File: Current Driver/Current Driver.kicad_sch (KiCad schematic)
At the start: 41 parts, among them Q1 BC817, Q2 D45H11G (n_b), Q3 BC807, Q4 D44H11(n_b), SW1 SW_Push, U1 ADA4622-2xCP, U2 ADA4622-2xCP

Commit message: Clean Schematic
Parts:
- removed D3: AS3BJ (n_b), Diode_SMD:D_SOD-523, symbol Diode:1N4148WT
- removed Q4: D44H11(n_b), symbol Simulation_SPICE:PNP
- removed R32, R33: 1kΩ, symbol Device:R
- removed SW1: SW_Push, symbol Switch:SW_Push
- removed unit 2 of U2
- added J1: Conn_01x03, symbol Connector_Generic:Conn_01x03
- added J2: Conn_01x02, symbol Connector_Generic:Conn_01x02
- added J3: Cewka, symbol Connector_Generic:Conn_01x02
- added Q4: NPN, symbol Simulation_SPICE:NPN
- added R22, R25, R27, R28, R29: R, symbol Device:R
- added unit 2 of U1
- renumbered C4 to C1, C6 to C2, C7 to C3, Q3 to Q2, Q2 to Q3, R6 to R1, R19 to R10, R5 to R11, R24 to R12, R12 to R13, R9 to R14, R29 to R15, R1 to R16, R21 to R17, R3 to R18, R18 to R19, R8 to R2, R2 to R20, R20 to R21, R7 to R23, R16 to R24, R28 to R26, R13 to R3, R17 to R30, R9 to R4, R14 to R5, R11 to R6, R15 to R7, R4 to R8, R10 to R9
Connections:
- net +VCC: now also R22.1; no longer Q3.3 (E)
- net +Vop: now also J1.3 (Pin_3)
- net -VCC: now also R25.2
- net -Vop: now also J1.1 (Pin_1)
- net GND: now also R26.2, J1.2 (Pin_2), J2.2 (Pin_2), R27.2, R28.2, R29.2; no longer R26.1, R7.2
- net DRIVING_OUTPUT: now reaches F1.1, R23.2, R24.1
- net DRIVER_OUTPUT: now reaches F1.2, R30.1
- net DRIVER_OUTPUT: now also J3.2 (Pin_2)
- net at Q2.2 (E), R24.2: now also Q4.1 (C)
- net at Q2.3 (C), R21.1: now also Q4.2 (B)
- net at R30.2: now also R15.1, R26.1, J3.1 (Pin_1), R27.1, R28.1, R29.1
- net at C1.2, R8.2, R9.2: now also U2.1; no longer U1.1
- net SIGNAL_INPUT: now reaches R6.1, R7.1
- net SIGNAL_INPUT: now also U2.3 (+); no longer U1.2 (-)
- net V_REF: now reaches C1.1, R4.1, R8.1
- net V_REF: now also U2.2 (-); no longer U1.3 (+)
- net at C2.1, R10.1: now also U1.2 (-); no longer U2.2 (-)
- net at C2.2, R11.1, R13.2: now also U1.1; no longer U2.1
- net at R11.2, R9.1: now also U1.3 (+); no longer U2.3 (+)
- net at C3.1, R10.2, R12.2: now also U1.7
- net at C3.2, R12.1, R14.2: now also U1.6 (-)
- net DRIVING_INPUT: now reaches D1.1 (K), D2.2 (A), R13.1
- net at R15.2: now also U1.5 (+)
- new net: Q3.3 (E), R22.2
- new net: Q4.3 (E), R25.1
- new net uC_SIGNAL: J2.1 (Pin_1), R7.2
- no-connect marks 2 -> 0
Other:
- company: (none) -> KN NaMi
- moved on the sheet: C1, C2, C3, D1, D2, F1, Q1, Q2, Q3, R10, R11, R12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

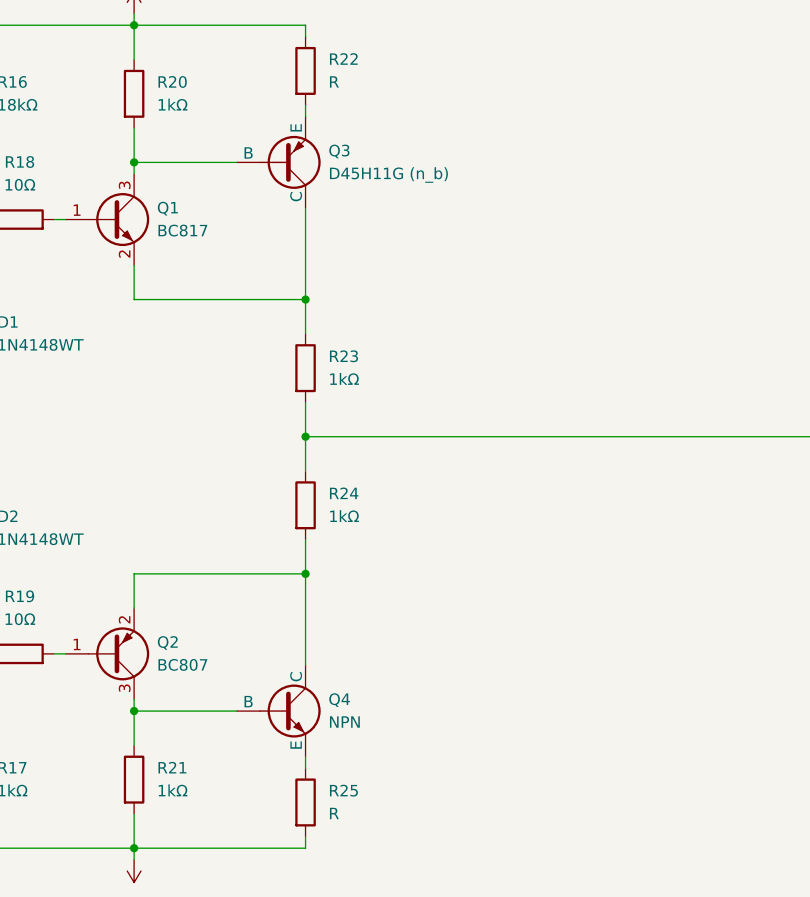
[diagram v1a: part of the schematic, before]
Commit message: Add Spice simulation
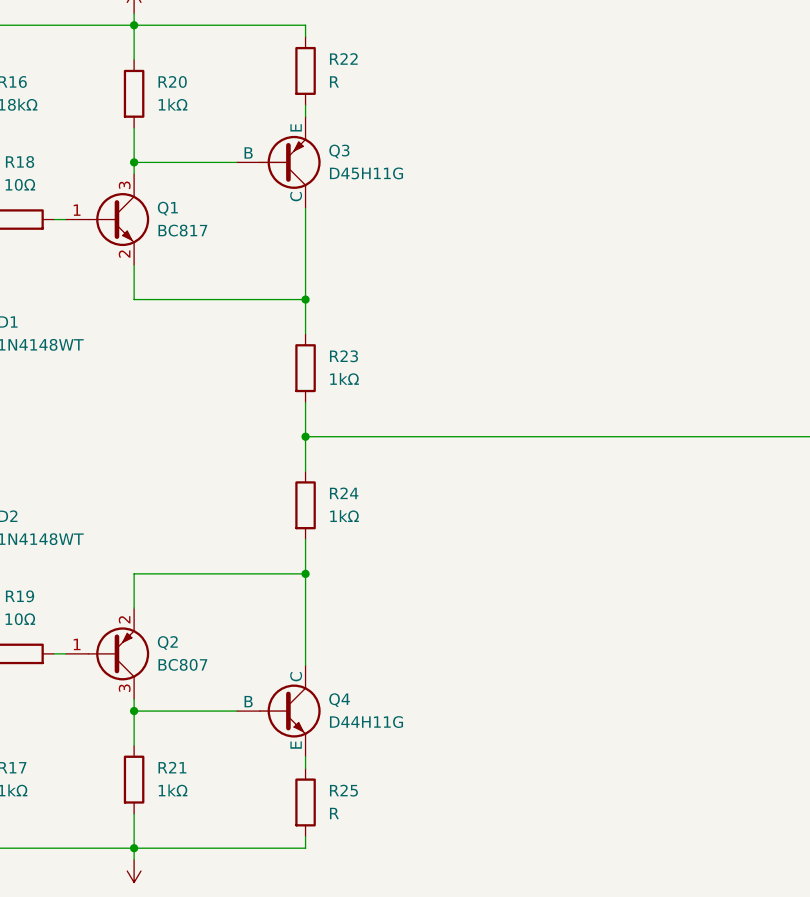
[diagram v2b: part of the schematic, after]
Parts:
- Q3: value D45H11G (n_b) -> D45H11G
- Q4: value NPN -> D44H11G
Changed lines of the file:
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@@
 			)
 		)
-		(property "Value" "D45H11G (n_b)"
+		(property "Value" "D45H11G"
 			(at 186.69 45.7199 0)
 			(effects
@@
 			)
 		)
-		(property "Value" "NPN"
+		(property "Value" "D44H11G"
 			(at 186.69 106.6799 0)
 			(effects

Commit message: edit schamatic update
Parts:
- added C4, C7: 100n, symbol Device:C
- added C5, C6: 47u, symbol Device:C
- added J4, J5: Screw_Terminal_01x03, symbol Connector:Screw_Terminal_01x03
- added Q5: D45H11, symbol Simulation_SPICE:PNP
- added Q6: MJD44H11, symbol Simulation_SPICE:NPN
- added R31: 300kΩ, symbol Device:R
- added R32: 10k, symbol Device:R
- added R33, R34: R, symbol Device:R
- C2: value 47pF -> 100pF
- C3: value 220pF -> 10pF
- R1: value 180Ω -> 300Ω
- R12: value 16kΩ -> 10k
- R15, R18, R19: value 10Ω -> 100
- R17: value 1kΩ -> 18k
- R2: value 1kΩ -> 300kΩ
- R22, R25: value R -> 430m
- R23, R24: value 1kΩ -> 430m
- R26: value 200mΩ -> 110mΩ
- R30: value 100kΩ -> 10
- R4: value 1kΩ -> 10kΩ
- R5: value 2kΩ -> 1,5kΩ
- R6: value 845Ω -> 3,6Ω
- R9: value 10kΩ -> 100Ω
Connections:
- net +VCC: now also Q3.3 (E), C4.1, C5.1, J4.1 (Pin_1), Q5.3 (E); no longer R22.1
- net -VCC: now also Q4.3 (E), C6.1, C7.1, J5.3 (Pin_3), Q6.3 (E); no longer R25.2
- net DRIVER_OUTPUT: now also R32.1
- net DRIVING_OUTPUT: now also R22.2, R25.1, R33.1, R34.2
- net GND: now also R6.2, C4.2, C5.2, C6.2, C7.2
- net SIGNAL_INPUT: now also R5.1
- net at R1.2: now also R31.1; no longer R2.1
- net at Q2.3 (C), Q4.2 (B), R21.1: now also J5.2 (Pin_2), Q6.2 (B)
- net at J3.1 (Pin_1), R15.1, R26.1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: now also R32.2
- net at Q1.3 (C), Q3.2 (B), R20.2: now also J4.2 (Pin_2), Q5.2 (B)
- new net: J5.1 (Pin_1), R33.2
- new net: J4.3 (Pin_3), R34.1
- new net: Q6.1 (C), R25.2
- new net: Q5.1 (C), R22.1
- new net: R2.1, R31.2
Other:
- moved on the sheet: F1, J3, Q3, Q4, R1, R16, R17, R2, R20, R21, R23, R24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

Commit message: Check & Edit Schematic
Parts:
- removed R30: 10, symbol Device:R
- removed R6: 3,6Ω, symbol Device:R
- added C10, C11, C8, C9: 25u, symbol Device:C_Polarized
- C1, C3, C4, C5, C6, C7: footprint (none) -> Capacitor_SMD:C_0805_2012Metric_Pad1.18x1.45mm_HandSolder
- C2: value 100pF -> C; footprint (none) -> Capacitor_SMD:C_0805_2012Metric_Pad1.18x1.45mm_HandSolder
- J2: value Conn_01x02 -> Input
- J3: value Cewka -> Load
- J4: value Screw_Terminal_01x03 -> VP BJT Conn
- J5: value Screw_Terminal_01x03 -> VN BJT Conn
- Q6: value MJD44H11 -> D44H11G
- R1, R10, R11, R12, R13, R14, R15, R16, R17, R18, R19, R20, R21, R22, R23, R24, R25, R3, R32, R33, R34, R4, R7, R8, R9: footprint (none) -> Resistor_SMD:R_0805_2012Metric_Pad1.20x1.40mm_HandSolder
- R2, R31: value 300kΩ -> 300Ω; footprint (none) -> Resistor_SMD:R_0805_2012Metric_Pad1.20x1.40mm_HandSolder
- R26: value 110mΩ -> 430mΩ; footprint (none) -> Resistor_SMD:R_0805_2012Metric_Pad1.20x1.40mm_HandSolder
- R27, R28, R29: value R -> 430mΩ; footprint (none) -> Resistor_SMD:R_0805_2012Metric_Pad1.20x1.40mm_HandSolder
- R5: value 1,5kΩ -> 1kΩ; footprint (none) -> Resistor_SMD:R_0805_2012Metric_Pad1.20x1.40mm_HandSolder
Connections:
- net +Vop is gone; now on net +VCC: J1.3 (Pin_3), U1.8 (V+), U1.9 (V+), U2.8 (V+), U2.9 (V+)
- net -Vop is gone; now on net -VCC: J1.1 (Pin_1), U1.4 (V-), U2.4 (V-)
- net +VCC: now also C6.1, C7.1, C11.1, C9.1; no longer C4.1, C5.1
- net -VCC: now also C4.1, C5.1, C10.2, C8.2; no longer C6.1, C7.1
- net GND: now also C10.1, C11.2, C8.1, C9.2
- net V_REF: now also R2.2, R3.1, R4.2; no longer C1.1, R4.1, R8.1, U2.2 (-)
- net VNEG_DRIV: now reaches J5.2 (Pin_2), Q2.3 (C), Q4.2 (B), Q6.2 (B), R21.1
- net CURRENT_FEEDBACK: now reaches J3.1 (Pin_1), R15.1, R26.1, R27.1, R28.1, R29.1, R32.2
- net VPOS_DRIV: now reaches J4.2 (Pin_2), Q1.3 (C), Q3.2 (B), Q5.2 (B), R20.2
- new net: C1.1, R4.1, R8.1, U2.2 (-)
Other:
- note added: "Complementary pair with Shiklai's pairs"
- note added: "Input signal divider"
- note added: "OpAmp power supply"
- note added: "P = 2 W"
- note added: "P = 400 mW"
- note added: "P = 45-50 W"
- note added: "Power coupling capacitors"
- note added: "Power input connector"
- note added: "Rz = 107,5 mΩ ~ 110 mΩ"
- note added: "Rz = 215 mΩ"
- note added: "Vref ~ 1,65 V"
- moved on the sheet: C4, C5, C6, C7, J1, R32, R4, R5, R9, U1C, U2C

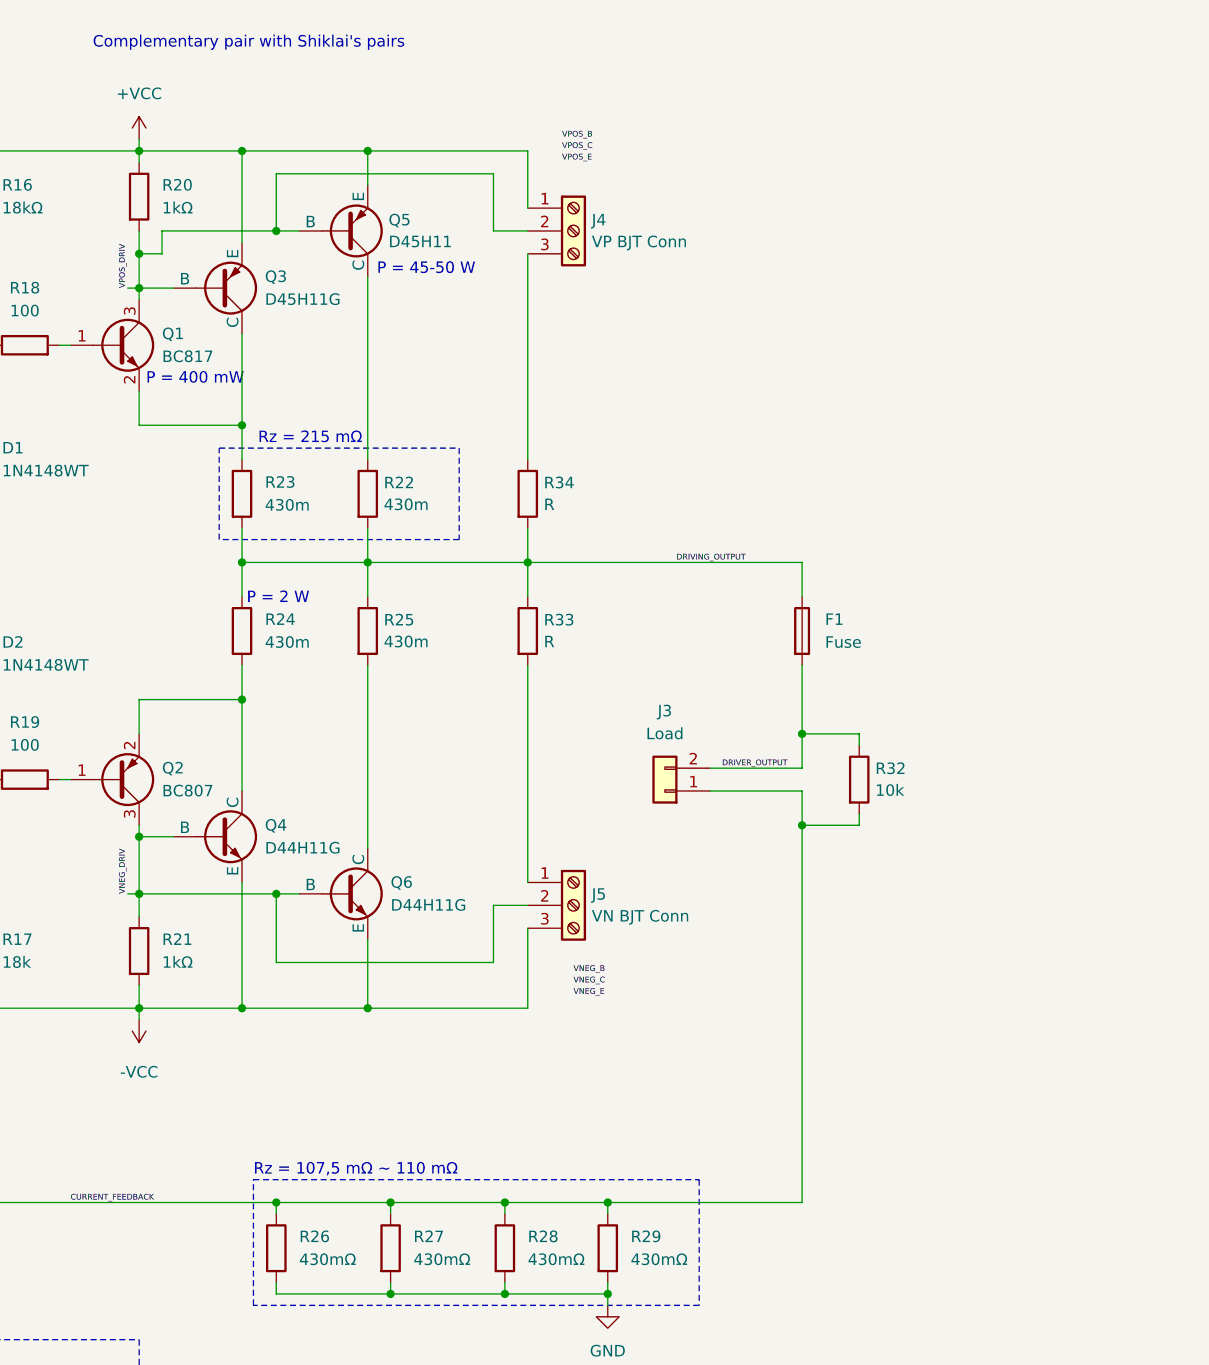
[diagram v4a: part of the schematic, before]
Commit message: schematic update
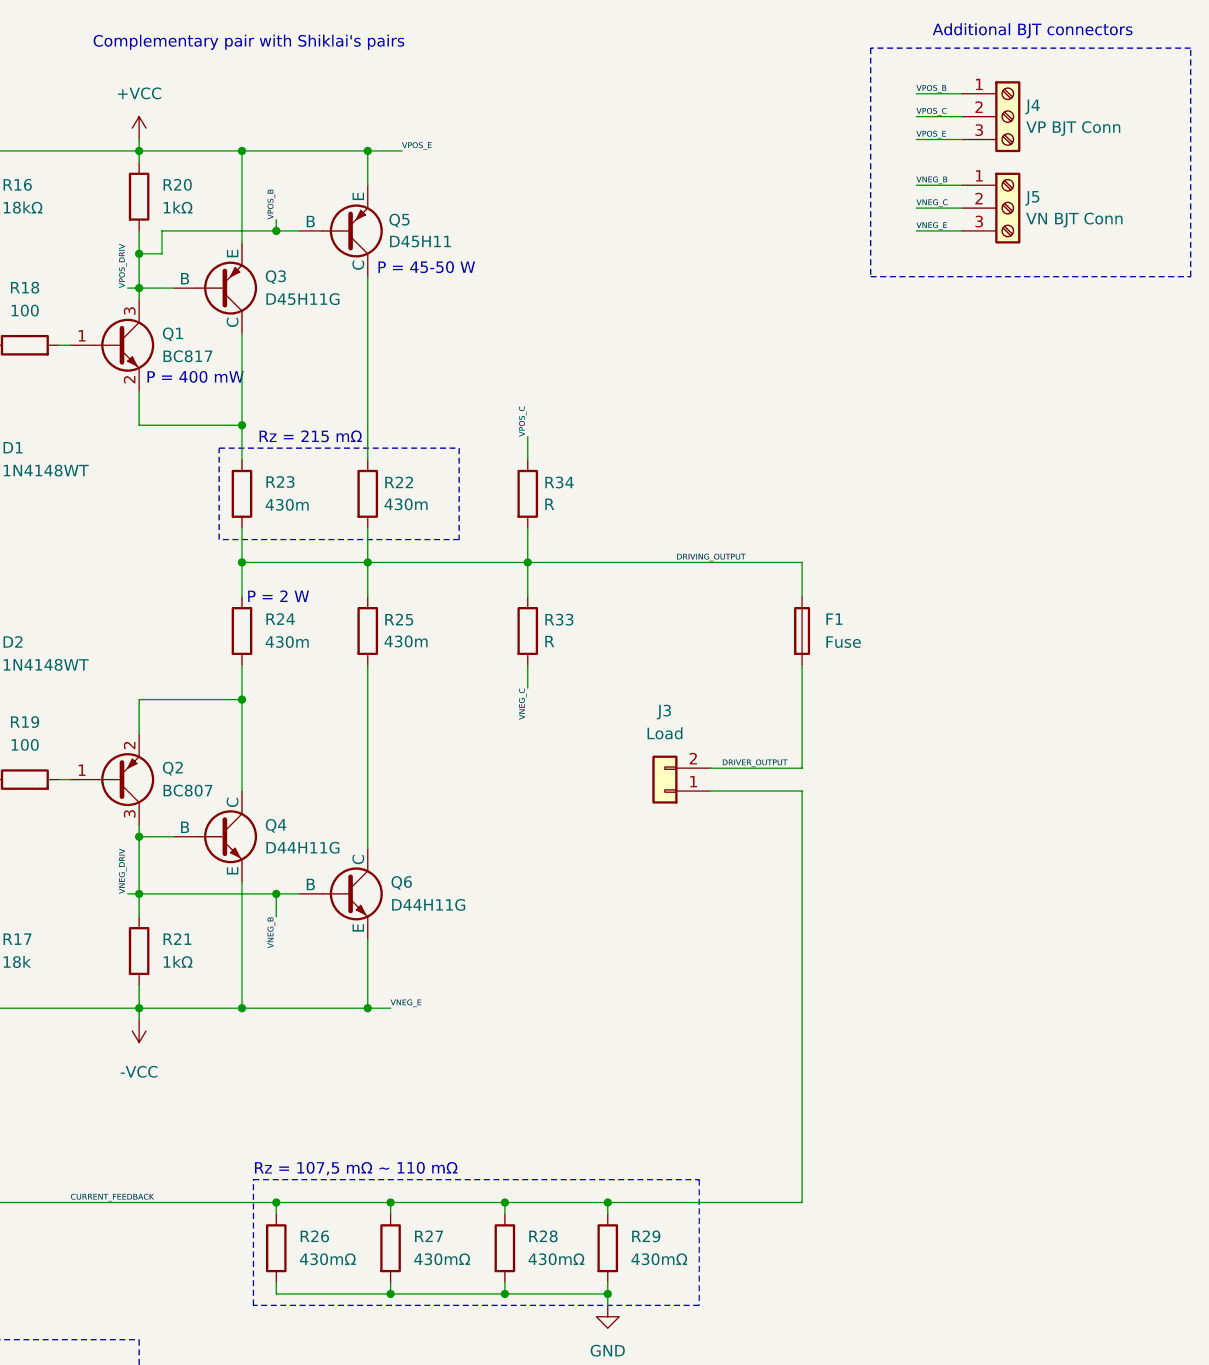
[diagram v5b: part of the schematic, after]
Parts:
- removed R32: 10k, Resistor_SMD:R_0805_2012Metric_Pad1.20x1.40mm_HandSolder, symbol Device:R
- C10, C11, C8, C9: footprint (none) -> Capacitor_SMD:CP_Elec_6.3x7.7
- F1: footprint (none) -> component_lib:2410 FUSE
- J4, J5: footprint (none) -> TerminalBlock:TerminalBlock_Xinya_XY308-2.54-3P_1x03_P2.54mm_Horizontal
- Q3, Q5, Q6: footprint (none) -> component_lib:TO254P1009X445X1985-3
- Q4: footprint (none) -> Package_TO_SOT_THT:TO-220-3_Vertical
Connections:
- net +VCC: now also J4.3 (Pin_3); no longer J4.1 (Pin_1)
- net VNEG_B: now also J5.1 (Pin_1), Q2.3 (C), Q4.2 (B), Q6.2 (B), R21.1
- net VNEG_C: now also J5.2 (Pin_2), R33.2
- net VPOS_B: now also J4.1 (Pin_1), Q1.3 (C), Q3.2 (B), Q5.2 (B), R20.2
- net VPOS_C: now also J4.2 (Pin_2), R34.1
- removed net VNEG_DRIV: J5.2 (Pin_2), Q2.3 (C), Q4.2 (B), Q6.2 (B), R21.1
- removed net VPOS_DRIV: J4.2 (Pin_2), Q1.3 (C), Q3.2 (B), Q5.2 (B), R20.2
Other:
- note added: "Additional BJT connectors"
- moved on the sheet: J4, J5
